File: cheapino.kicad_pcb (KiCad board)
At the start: 2 copper layers, 139 x 102.6 mm, 42 parts, among them K1 SW_Push, K10 SW_Push, K11 SW_Push, K12 SW_Push, K13 SW_Push, K14 SW_Push, K15 SW_Push, K16 SW_Push, K17 SW_Push, K18 SW_Push, K2 SW_Push, K3 SW_Push, K4 SW_Push, K5 SW_Push, K6 SW_Push, K7 SW_Push, K8 SW_Push, K9 SW_Push, U1 RP2040-Zero

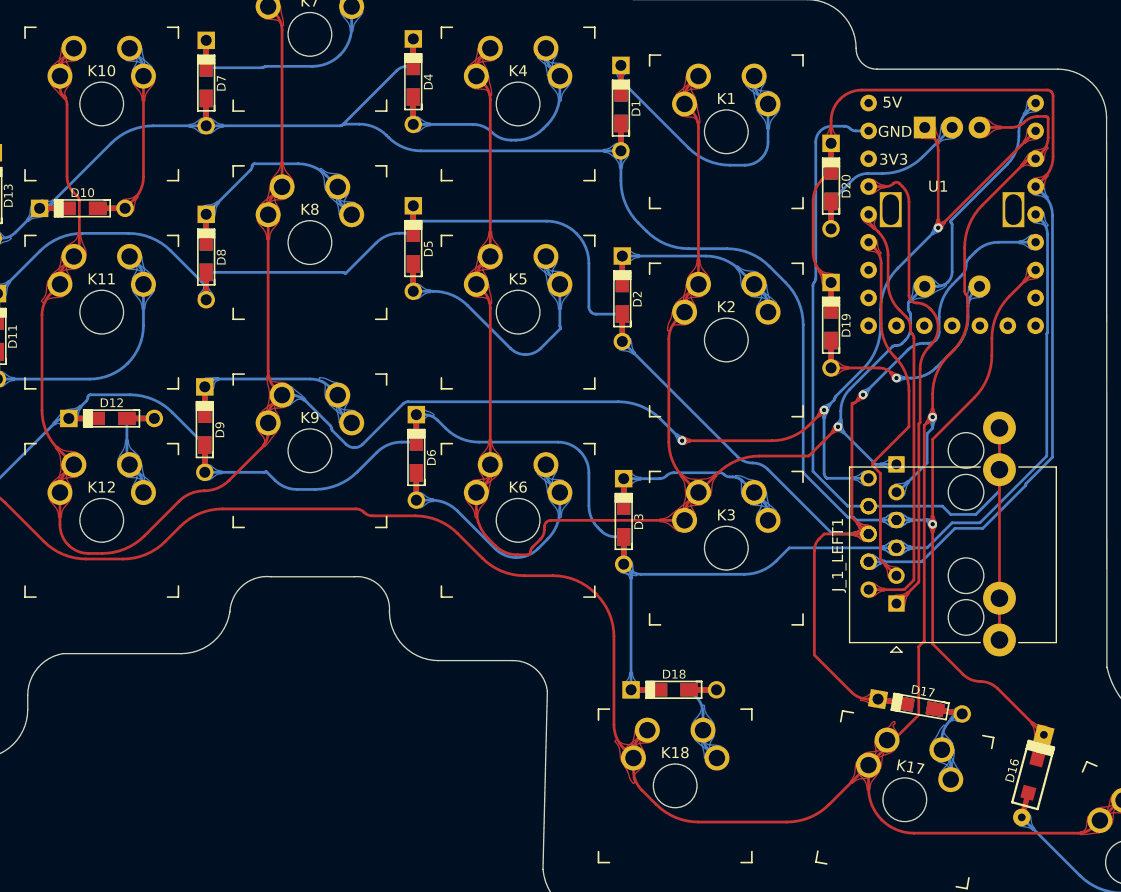
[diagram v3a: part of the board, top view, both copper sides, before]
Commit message: Fixed missing pads on one smb diode
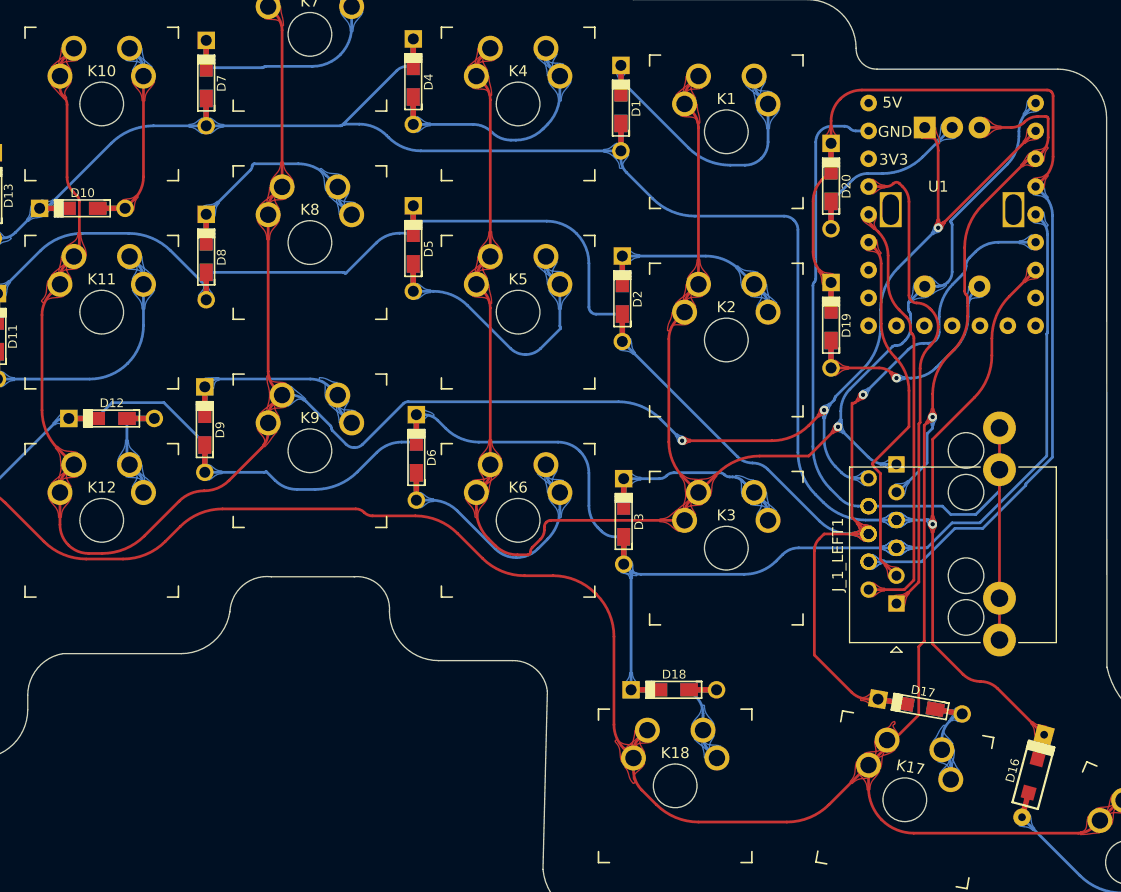
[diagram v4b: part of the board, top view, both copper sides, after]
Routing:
- net ROW_3: track 154.3 -> 151.3 mm
- net ROW_1: track 175.0 -> 177.3 mm
- net COL_2: track 222.7 -> 221.3 mm

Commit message: Hotswap support and solder jumpers
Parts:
- added D21: DIODE, keebio:Diode-dual, F.Cu at (266.4, 91.9)
- added JP1: SolderJumper_2_Open, Jumper:SolderJumper-2_P1.3mm_Open_TrianglePad1.0x1.5mm, F.Cu at (292.8, 41.6)
- added JP2: SolderJumper_2_Open, Jumper:SolderJumper-2_P1.3mm_Open_TrianglePad1.0x1.5mm, F.Cu at (292.8, 45.1)
- added JP3: SolderJumper_2_Open, Jumper:SolderJumper-2_P1.3mm_Open_TrianglePad1.0x1.5mm, F.Cu at (292.8, 48.7)
- added JP4: SolderJumper_2_Open, Jumper:SolderJumper-2_P1.3mm_Open_TrianglePad1.0x1.5mm, F.Cu at (292.8, 52.2)
- added JP5: SolderJumper_2_Open, Jumper:SolderJumper-2_P1.3mm_Open_TrianglePad1.0x1.5mm, F.Cu at (292.8, 55.8)
- added JP6: SolderJumper_2_Open, Jumper:SolderJumper-2_P1.3mm_Open_TrianglePad1.0x1.5mm, F.Cu at (292.8, 59.3)
- added JP7: SolderJumper_2_Open, Jumper:SolderJumper-2_P1.3mm_Open_TrianglePad1.0x1.5mm, F.Cu at (292.8, 62.9)
- ENC1, J_2_RIGHT1: moved to F.Cu
- K1, K10, K11, K12, K13, K14, K15, K16, K17, K18, K2, K3, K4, K5, K6, K7, K8, K9: footprint project_footprints:SW_MX_reversible_minimal -> project_footprints:Kailh_socket_MX_optional_reversible
- moved D15 197.1 mm to (266.4, 78.5), turned to 0 degrees
- moved D14 196.6 mm to (266.4, 75.9), turned to 0 degrees
- moved D11 188.4 mm to (266.4, 67.9), turned to 0 degrees
- moved D13 188.4 mm to (266.4, 73.2), turned to 0 degrees
- moved K15 184.9 mm to (251.8, 80.2)
- moved K14 184.5 mm to (251.8, 64.0)
- moved K13 184.1 mm to (251.8, 47.9)
- moved D10 180.2 mm to (266.4, 65.2), turned to 0 degrees
- moved D12 178.5 mm to (266.4, 70.5), turned to 0 degrees
- moved D9 171.2 mm to (266.4, 62.5), turned to 0 degrees
- moved D8 169.5 mm to (266.4, 59.8), turned to 0 degrees
- moved D7 168.9 mm to (266.4, 57.2), turned to 0 degrees
- moved D6 154.5 mm to (266.4, 54.5), turned to 0 degrees
- moved D5 151.5 mm to (266.4, 51.8), turned to 0 degrees
- moved K10 150.5 mm to (234.1, 96.3)
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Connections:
- D19 pad 1: ROW_4 -> COL_2
- D19 pad 2: Net-(D19-Pad2) -> Net-(D19-A)
- D20 pad 1: ROW_4 -> COL_3
- D20 pad 2: Net-(D20-Pad2) -> Net-(D20-A)
- ENC1 pad A: COL_2 -> Net-(D19-A)
- ENC1 pad B: COL_3 -> Net-(D20-A)
- ENC1 pad C: Net-(D20-Pad2) -> ROW_4
- ENC1 pad S1: Net-(D19-Pad2) -> Net-(D21-A)
- ENC1 pad S2: COL_1 -> ROW_4
- J_1_LEFT1 pad 4: ROW_4 -> REMOTE_ROW_1
- J_1_LEFT1 pad 5: ROW_3 -> REMOTE_ROW_2
- J_1_LEFT1 pad 6: ROW_2 -> REMOTE_ROW_3
- J_1_LEFT1 pad 7: ROW_1 -> REMOTE_ROW_4
- J_2_RIGHT1 pad 1: COL_1 -> LOCAL_COL_1
- J_2_RIGHT1 pad 2: COL_2 -> LOCAL_COL_2
- J_2_RIGHT1 pad 3: COL_3 -> LOCAL_COL_3
- J_2_RIGHT1 pad 4: GND -> LOCAL_ROW_1
- J_2_RIGHT1 pad 5: ROW_1 -> LOCAL_ROW_2
- J_2_RIGHT1 pad 6: ROW_2 -> LOCAL_ROW_3
- J_2_RIGHT1 pad 7: ROW_3 -> LOCAL_ROW_4
- J_2_RIGHT1 pad 8: ROW_4 -> GND
- U1 pad 0: COL_1 -> REMOTE_COL_1
- U1 pad 1: COL_2 -> REMOTE_COL_2
- U1 pad 14: unconnected-(U1-Pad14) -> ROW_3
- U1 pad 15: unconnected-(U1-Pad15) -> ROW_2
- U1 pad 2: COL_3 -> REMOTE_COL_3
- U1 pad 26: unconnected-(U1-Pad26) -> ROW_1
- U1 pad 27: REMOTE_COL_3 -> COL_3
- U1 pad 28: REMOTE_COL_2 -> COL_2
- U1 pad 29: REMOTE_COL_1 -> COL_1
- U1 pad 3: ROW_4 -> REMOTE_ROW_1
- U1 pad 4: ROW_3 -> REMOTE_ROW_2
- U1 pad 5: ROW_2 -> REMOTE_ROW_3
- U1 pad 6: ROW_1 -> REMOTE_ROW_4
- U1 pad 8: unconnected-(U1-Pad8) -> ROW_4
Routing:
- net COL_3: track 288.1 -> 0.00 mm, vias 1 -> 0
- net COL_2: track 221.3 -> 0.00 mm, vias 3 -> 0
- net ROW_1: track 177.3 -> 0.00 mm, vias 1 -> 0
- net COL_1: track 171.7 -> 0.00 mm, vias 1 -> 0
- net ROW_2: track 164.6 -> 0.00 mm, vias 1 -> 0
- net ROW_3: track 151.3 -> 0.00 mm
- net ROW_4: track 90.3 -> 0.00 mm
- net GND: track 76.3 -> 0.00 mm
- net REMOTE_COL_1: track 44.3 -> 0.00 mm
- net REMOTE_COL_2: track 39.1 -> 0.00 mm
- net REMOTE_COL_3: track 33.7 -> 0.00 mm
- net Net-(D1-K): track 25.2 -> 0.00 mm
- net Net-(D5-A): track 23.4 -> 0.00 mm
- net Net-(D11-A): track 22.8 -> 0.00 mm
- net Net-(D6-A): track 21.9 -> 0.00 mm
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- removed copper zone on B.Cu, net GND
- removed copper zone on F.Cu, net GND
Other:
- board text removed: "3V3"
- board text removed: "5V"
- board text removed: "Cheapino"
- board text removed: "GND"

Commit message: V2 First draft
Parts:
- ENC1, JP1, JP2, JP3, JP4, JP5, JP6, JP7, J_2_RIGHT1: moved to B.Cu
- moved D15 197.9 mm to (69.6, 99.5), turned to 180 degrees
- moved D13 196.6 mm to (69.9, 80.5), turned to 180 degrees
- moved K15 184.9 mm to (69.0, 108.3)
- moved K14 184.5 mm to (69.0, 89.3)
- moved K13 184.1 mm to (69.0, 70.3)
- moved D14 183.3 mm to (83.6, 89.0), turned to 180 degrees
- moved D10 182.9 mm to (83.6, 70.0), turned to 180 degrees
- moved D12 173.5 mm to (93.9, 89.0), turned to 180 degrees
- moved D11 164.5 mm to (102.6, 82.3), turned to 180 degrees
- moved D7 161.6 mm to (105.0, 63.3), turned to 180 degrees
- moved D8 154.9 mm to (113.2, 82.3), turned to 180 degrees
- moved JP1 151.1 mm to (156.7, 107.1), turned to 90 degrees
- moved K10 150.5 mm to (88.0, 60.3)
- moved K11 149.8 mm to (88.0, 79.3)
- moved K12 149.2 mm to (88.0, 98.3)
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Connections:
- JP1 pad 2: LOCAL_COL_1 -> R_COL_1
- JP2 pad 2: LOCAL_COL_2 -> R_COL_2
- JP3 pad 2: LOCAL_COL_3 -> R_COL_3
- JP4 pad 2: LOCAL_ROW_1 -> R_ROW_1
- JP5 pad 2: LOCAL_ROW_2 -> R_ROW_3
- JP6 pad 2: LOCAL_ROW_3 -> R_ROW_2
- JP7 pad 2: LOCAL_ROW_4 -> R_ROW_4
- J_1_LEFT1 pad 1: REMOTE_COL_1 -> GND
- J_1_LEFT1 pad 2: REMOTE_COL_2 -> R_COL_1
- J_1_LEFT1 pad 3: REMOTE_COL_3 -> R_COL_2
- J_1_LEFT1 pad 4: REMOTE_ROW_1 -> R_COL_3
- J_1_LEFT1 pad 5: REMOTE_ROW_2 -> R_ROW_1
- J_1_LEFT1 pad 6: REMOTE_ROW_3 -> R_ROW_2
- J_1_LEFT1 pad 7: REMOTE_ROW_4 -> R_ROW_3
- J_1_LEFT1 pad 8: GND -> R_ROW_4
- J_2_RIGHT1 pad 1: LOCAL_COL_1 -> GND
- J_2_RIGHT1 pad 2: LOCAL_COL_2 -> R_ROW_4
- J_2_RIGHT1 pad 3: LOCAL_COL_3 -> R_ROW_3
- J_2_RIGHT1 pad 4: LOCAL_ROW_1 -> R_ROW_2
- J_2_RIGHT1 pad 5: LOCAL_ROW_2 -> R_ROW_1
- J_2_RIGHT1 pad 6: LOCAL_ROW_3 -> R_COL_3
- J_2_RIGHT1 pad 7: LOCAL_ROW_4 -> R_COL_2
- J_2_RIGHT1 pad 8: GND -> R_COL_1
- U1 pad 0: REMOTE_COL_1 -> R_COL_1
- U1 pad 1: REMOTE_COL_2 -> R_COL_2
- U1 pad 14: ROW_3 -> COL_1
- U1 pad 15: ROW_2 -> COL_2
- U1 pad 2: REMOTE_COL_3 -> R_COL_3
- U1 pad 26: ROW_1 -> COL_3
- U1 pad 27: COL_3 -> ROW_1
- U1 pad 28: COL_2 -> ROW_2
- U1 pad 29: COL_1 -> ROW_3
- U1 pad 3: REMOTE_ROW_1 -> R_ROW_1
- U1 pad 4: REMOTE_ROW_2 -> R_ROW_2
- U1 pad 5: REMOTE_ROW_3 -> R_ROW_3
- U1 pad 6: REMOTE_ROW_4 -> R_ROW_4
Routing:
- net COL_3: track 0.00 -> 336.8 mm, vias 0 -> 3
- net COL_2: track 0.00 -> 259.3 mm, vias 0 -> 3
- net COL_1: track 0.00 -> 229.7 mm, vias 0 -> 2
- net ROW_2: track 0.00 -> 208.8 mm, vias 0 -> 2
- net ROW_3: track 0.00 -> 178.4 mm, vias 0 -> 2
- net ROW_1: track 0.00 -> 158.7 mm, vias 0 -> 2
- net R_COL_1: track 0.00 -> 59.1 mm
- net R_COL_3: track 0.00 -> 56.9 mm
- net R_ROW_2: track 0.00 -> 55.6 mm
- net R_COL_2: track 0.00 -> 55.1 mm
- net ROW_4: track 0.00 -> 53.9 mm, vias 0 -> 1
- net R_ROW_4: track 0.00 -> 49.1 mm, vias 0 -> 1
- net R_ROW_1: track 0.00 -> 48.0 mm
- net R_ROW_3: track 0.00 -> 43.5 mm
- net Net-(D2-K): track 0.00 -> 43.1 mm
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- added copper zone on B.Cu, net GND
- added copper zone on F.Cu, net GND
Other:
- outline, holes or cut-outs redrawn
- board text added: "Cheapino v2"
- board text added: "Solder right side only"

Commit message: Ordered prototype
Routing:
- net COL_3: track 336.8 -> 343.4 mm
- net COL_1: track 229.7 -> 229.2 mm
- net GND: vias 17 -> 19
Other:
- board size 139 x 102.6 mm -> 132.5 x 95.1 mm

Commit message: M2 Mounting holes
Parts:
- added REF**: MountingHole_2.2mm_M2, MountingHole:MountingHole_2.2mm_M2, F.Cu at (153.9, 71.6)
- added REF**: MountingHole_2.2mm_M2, MountingHole:MountingHole_2.2mm_M2, F.Cu at (169.2, 132.6)
- moved D2 9.21 mm to (136.1, 81.4), turned to 90 degrees
- moved D1 5.32 mm to (145.3, 72.6)
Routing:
- net ROW_1: track 158.7 -> 138.6 mm
- net Net-(D2-K): track 43.1 -> 36.6 mm
- net Net-(D1-K): track 27.7 -> 30.0 mm
- net ROW_2: track 208.8 -> 207.0 mm
- net Net-(D17-A): track 37.4 -> 36.4 mm
- net R_ROW_4: track 49.1 -> 48.6 mm
- net GND: vias 19 -> 23
